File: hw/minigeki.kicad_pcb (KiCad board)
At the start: 2 copper layers, 52 x 56.1 mm, 29 parts, among them J1 USB_C_Receptacle_USB2.0, J2 Conn_01x02, U1 NCP1117-3.3_SOT223, U2 W25Q128JVS, U3 RP2040, Y1 ABLS-12.000MHZ-B4-T

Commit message: hw: finish main routing
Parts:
- added C17: 100n, Capacitor_SMD:C_0402_1005Metric, F.Cu at (52.7, 87.0)
- added C18: 100n, Capacitor_SMD:C_0402_1005Metric, B.Cu at (37.5, 106.0)
- added C19: 100n, Capacitor_SMD:C_0402_1005Metric, F.Cu at (43.8, 137.8)
- added C20: 100n, Capacitor_SMD:C_0402_1005Metric, F.Cu at (62.9, 137.8)
- added C21: 100n, Capacitor_SMD:C_0402_1005Metric, F.Cu at (81.9, 137.8)
- added C22: 100n, Capacitor_SMD:C_0402_1005Metric, F.Cu at (120.0, 137.8)
- added C23: 100n, Capacitor_SMD:C_0402_1005Metric, F.Cu at (139.1, 137.8)
- added C24: 100n, Capacitor_SMD:C_0402_1005Metric, F.Cu at (158.1, 137.8)
- added C25: 100n, Capacitor_SMD:C_0402_1005Metric, B.Cu at (165.7, 107.3)
- added C26: 100n, Capacitor_SMD:C_0402_1005Metric, F.Cu at (156.8, 87.0)
- added D1: SK6812MINI, LED_SMD:LED_SK6812MINI_PLCC4_3.5x3.5mm_P1.75mm, F.Cu at (49.5, 90.2)
- added D10: SK6812MINI, LED_SMD:LED_SK6812MINI_PLCC4_3.5x3.5mm_P1.75mm, F.Cu at (153.7, 90.2)
- added D2: SK6812MINI, LED_SMD:LED_SK6812MINI_PLCC4_3.5x3.5mm_P1.75mm, B.Cu at (34.3, 106.7)
- added D3: SK6812MINI, LED_SMD:LED_SK6812MINI_PLCC4_3.5x3.5mm_P1.75mm, F.Cu at (44.5, 134.6)
- added D4: SK6812MINI, LED_SMD:LED_SK6812MINI_PLCC4_3.5x3.5mm_P1.75mm, F.Cu at (63.5, 134.6)
- added D5: SK6812MINI, LED_SMD:LED_SK6812MINI_PLCC4_3.5x3.5mm_P1.75mm, F.Cu at (82.5, 134.6)
- added D6: SK6812MINI, LED_SMD:LED_SK6812MINI_PLCC4_3.5x3.5mm_P1.75mm, F.Cu at (120.7, 134.6)
- added D7: SK6812MINI, LED_SMD:LED_SK6812MINI_PLCC4_3.5x3.5mm_P1.75mm, F.Cu at (139.7, 134.6)
- added D8: SK6812MINI, LED_SMD:LED_SK6812MINI_PLCC4_3.5x3.5mm_P1.75mm, F.Cu at (158.8, 134.7)
- added D9: SK6812MINI, LED_SMD:LED_SK6812MINI_PLCC4_3.5x3.5mm_P1.75mm, B.Cu at (168.9, 106.7)
- added RV1: PTA4543-2015DPB103, PTAXX33:PTAXX43, F.Cu at (101.6, 101.6)
- added STAB1: Stabilizer_Cherry_MX_2.00u, Mounting_Keyboard_Stabilizer:Stabilizer_Cherry_MX_2.00u, F.Cu at (49.5, 84.5)
- added STAB2: Stabilizer_Cherry_MX_2.00u, Mounting_Keyboard_Stabilizer:Stabilizer_Cherry_MX_2.00u, F.Cu at (153.7, 84.5)
- added SW1: LEFT_R, Switch_Keyboard_Hotswap_Kailh:SW_Hotswap_Kailh_MX_1.00u, F.Cu at (44.5, 129.5)
- added SW10: RIGHT_WALL, Switch_Keyboard_Hotswap_Kailh:SW_Hotswap_Kailh_MX_2.00u, F.Cu at (153.7, 85.1)
- added SW11: MACRO_1, Button_Switch_SMD:SW_SPST_PTS810, F.Cu at (49.5, 106.7)
- added SW12: MACRO_2, Button_Switch_SMD:SW_SPST_PTS810, F.Cu at (153.7, 106.7)
- added SW2: LEFT_G, Switch_Keyboard_Hotswap_Kailh:SW_Hotswap_Kailh_MX_1.00u, F.Cu at (63.5, 129.5)
- added SW3: LEFT_B, Switch_Keyboard_Hotswap_Kailh:SW_Hotswap_Kailh_MX_1.00u, F.Cu at (82.5, 129.5)
- added SW4: LEFT_START, Switch_Keyboard_Hotswap_Kailh:SW_Hotswap_Kailh_MX_1.00u, F.Cu at (81.3, 76.2)
- added SW5: LEFT_WALL, Switch_Keyboard_Hotswap_Kailh:SW_Hotswap_Kailh_MX_2.00u, F.Cu at (49.5, 85.1)
- added SW6: RIGHT_R, Switch_Keyboard_Hotswap_Kailh:SW_Hotswap_Kailh_MX_1.00u, F.Cu at (120.7, 129.5)
- added SW7: RIGHT_G, Switch_Keyboard_Hotswap_Kailh:SW_Hotswap_Kailh_MX_1.00u, F.Cu at (139.7, 129.5)
- added SW8: RIGHT_B, Switch_Keyboard_Hotswap_Kailh:SW_Hotswap_Kailh_MX_1.00u, F.Cu at (158.8, 129.5)
- added SW9: RIGHT_START, Switch_Keyboard_Hotswap_Kailh:SW_Hotswap_Kailh_MX_1.00u, F.Cu at (121.9, 76.2)
- C1, C10, C11, C12, C13, C14, C15, C16, C2, C3, C4, C5, C6, C7, C8, C9, J1, J2, R1, R2, R3, R4, R5, R6, R7, U1, U2, U3, Y1: moved to B.Cu
- moved R2 21.0 mm to (110.5, 82.3)
- moved C4 18.1 mm to (91.0, 89.0), turned to 180 degrees
- moved R1 18.0 mm to (109.0, 82.3)
- moved U1 16.0 mm to (92.0, 82.8)
- moved C1 15.9 mm to (92.1, 76.5), turned to 180 degrees
- moved J2 15.5 mm to (106.6, 77.3), turned to 90 degrees
- moved U2 13.9 mm to (107.0, 87.3), turned to 180 degrees
- moved R6 13.8 mm to (93.1, 70.3)
- moved C11 13.0 mm to (106.5, 97.0), turned to 0 degrees
- moved C12 13.0 mm to (93.5, 101.2), turned to 180 degrees
- moved C13 13.0 mm to (106.5, 101.2), turned to 0 degrees
- moved C15 13.0 mm to (93.5, 96.0), turned to 180 degrees
- moved C16 13.0 mm to (93.5, 94.6), turned to 180 degrees
- moved R7 11.1 mm to (105.6, 70.3)
- moved C10 8.00 mm to (96.0, 93.5)
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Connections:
- U3 pad 11: /GPIO8 -> unconnected-(U3-Pad11)
- U3 pad 12: /GPIO9 -> unconnected-(U3-Pad12)
- U3 pad 13: /GPIO10 -> unconnected-(U3-Pad13)
- U3 pad 14: /GPIO11 -> unconnected-(U3-Pad14)
- U3 pad 15: /GPIO12 -> /RIGHT_B
- U3 pad 16: /GPIO13 -> /RIGHT_G
- U3 pad 17: /GPIO14 -> /RIGHT_R
- U3 pad 18: /GPIO15 -> unconnected-(U3-Pad18)
- U3 pad 2: /GPIO0 -> unconnected-(U3-Pad2)
- U3 pad 27: /GPIO16 -> unconnected-(U3-Pad27)
- U3 pad 28: /GPIO17 -> unconnected-(U3-Pad28)
- U3 pad 29: /GPIO18 -> /LEFT_B
- U3 pad 3: /GPIO1 -> unconnected-(U3-Pad3)
- U3 pad 30: /GPIO19 -> /LEFT_G
- U3 pad 31: /GPIO20 -> /LEFT_R
- U3 pad 32: /GPIO21 -> unconnected-(U3-Pad32)
- U3 pad 34: /GPIO22 -> unconnected-(U3-Pad34)
- U3 pad 35: /GPIO23 -> unconnected-(U3-Pad35)
- U3 pad 36: /GPIO24 -> /LED_DIN
- U3 pad 37: /GPIO25 -> unconnected-(U3-Pad37)
- U3 pad 39: /GPIO27_ADC1 -> /MACRO_1
- U3 pad 4: /GPIO2 -> unconnected-(U3-Pad4)
- U3 pad 40: /GPIO28_ADC2 -> /LEFT_WALL
- U3 pad 41: /GPIO29_ADC3 -> /LEFT_START
- U3 pad 5: /GPIO3 -> unconnected-(U3-Pad5)
- U3 pad 6: /GPIO4 -> /RIGHT_START
- U3 pad 7: /GPIO5 -> /RIGHT_WALL
- U3 pad 8: /GPIO6 -> /MACRO2
- U3 pad 9: /GPIO7 -> unconnected-(U3-Pad9)
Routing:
- net /LEFT_R: track 0.00 -> 74.1 mm
- net /LEFT_WALL: track 0.00 -> 61.9 mm
- net /RIGHT_B: track 0.00 -> 60.0 mm
- net /LEFT_G: track 0.00 -> 51.5 mm
- net /MACRO2: track 0.00 -> 50.4 mm, vias 0 -> 1
- net /RIGHT_WALL: track 0.00 -> 50.3 mm
- net /LED_DIN: track 0.00 -> 49.6 mm, vias 0 -> 1
- net /MACRO_1: track 0.00 -> 47.9 mm, vias 0 -> 1
- net /RIGHT_G: track 0.00 -> 41.0 mm
- net Net-(D5-Pad1): track 0.00 -> 35.3 mm
- net /LEFT_START: track 0.00 -> 35.2 mm
- net /LEFT_B: track 0.00 -> 33.4 mm
- net Net-(D8-Pad1): track 0.00 -> 33.4 mm, vias 0 -> 1
- net /RIGHT_START: track 0.00 -> 32.6 mm
- net Net-(D2-Pad1): track 0.00 -> 30.8 mm, vias 0 -> 1
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- added copper zone on B.Cu, net +1V1
- added copper zone on B.Cu, net +3V3
- added copper zone on B.Cu, net VBUS
- removed copper zone on F.Cu, net +1V1
- removed copper zone on F.Cu, net +3V3
- removed copper zone on F.Cu, net VBUS
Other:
- board size 52 x 56.1 mm -> 146.7 x 78.2 mm

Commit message: hw: final routing pass
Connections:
- SW5 pad 2: unconnected-(SW5-Pad2) -> GND
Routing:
- net GND: track 52.1 -> 115.6 mm, vias 30 -> 60
- net +3V3: track 48.1 -> 64.1 mm, vias 0 -> 2
- net /MACRO2: track 50.4 -> 54.5 mm
- net /MACRO_1: track 47.9 -> 52.0 mm

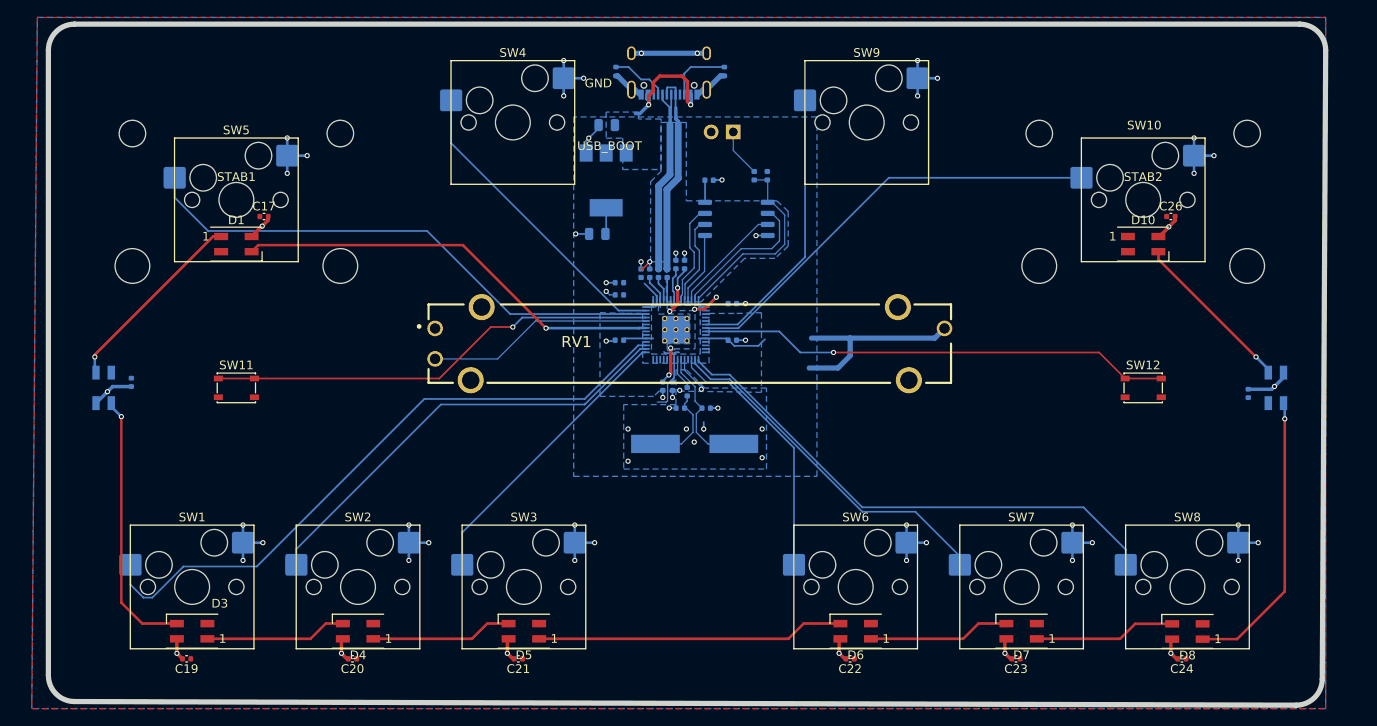
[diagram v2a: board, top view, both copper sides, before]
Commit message: hw: add mounting holes
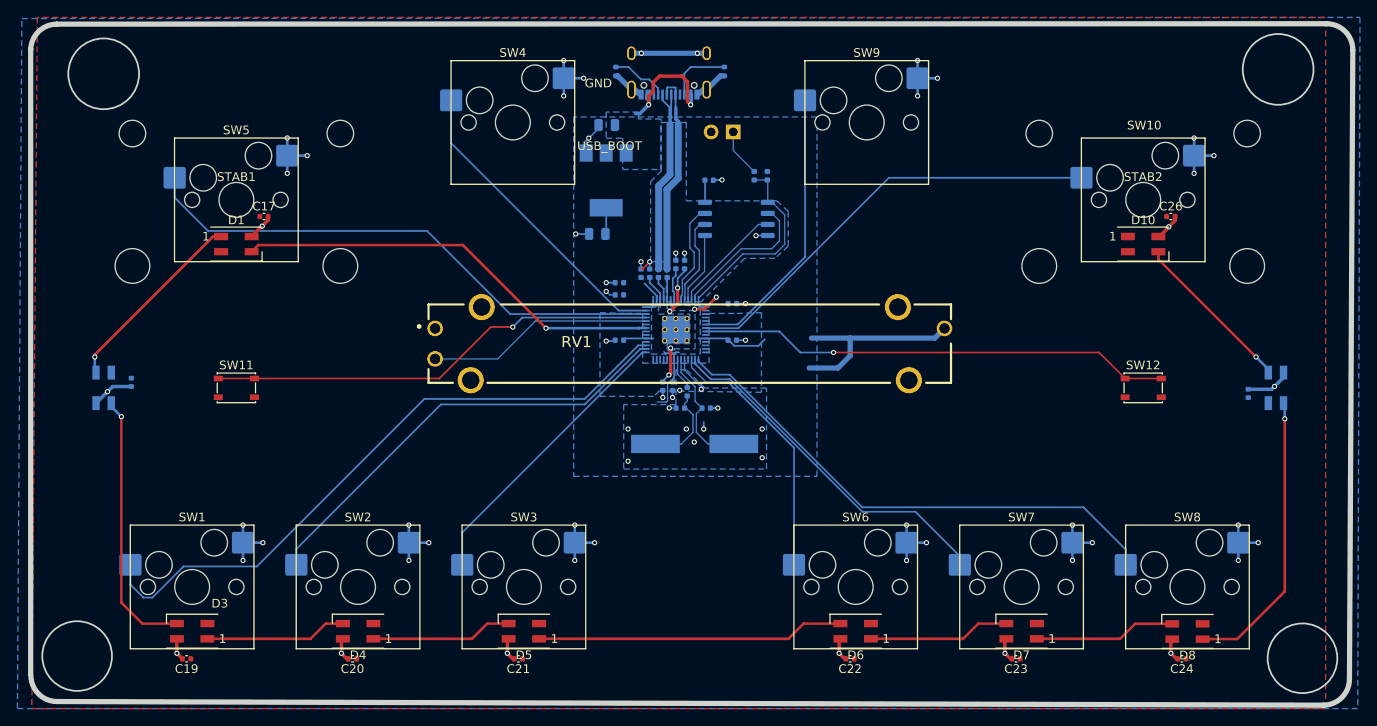
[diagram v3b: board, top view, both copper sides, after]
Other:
- board size 146.7 x 78.2 mm -> 151.8 x 78.3 mm
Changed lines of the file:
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@@
     (fp_line (start -2 0) (end 2 0) (layer "Dwgs.User") (width 0.1))
     (fp_line (start 0 2) (end 0 -2) (layer "Dwgs.User") (width 0.1))
+    (fp_line (start 15.313 -5.53) (end 8.563 -5.53) (layer "Eco1.User") (width 0.1))
     (fp_line (start 15.313 6.77) (end 15.313 -5.53) (layer "Eco1.User") (width 0.1))
+    (fp_line (start -15.313 -5.53) (end -15.313 6.77) (layer "Eco1.User") (width 0.1))
+    (fp_line (start -15.313 6.77) (end -8.563 6.77) (layer "Eco1.User") (width 0.1))
+    (fp_line (start -8.563 6.77) (end -8.563 -5.53) (layer "Eco1.User") (width 0.1))
     (fp_line (start -8.563 -5.53) (end -15.313 -5.53) (layer "Eco1.User") (width 0.1))
     (fp_line (start 8.563 -5.53) (end 8.563 6.77) (layer "Eco1.User") (width 0.1))
-    (fp_line (start -8.563 6.77) (end -8.563 -5.53) (layer "Eco1.User") (width 0.1))
     (fp_line (start 8.563 6.77) (end 15.313 6.77) (layer "Eco1.User") (width 0.1))
-    (fp_line (start -15.313 -5.53) (end -15.313 6.77) (layer "Eco1.User") (width 0.1))
-    (fp_line (start 15.313 -5.53) (end 8.563 -5.53) (layer "Eco1.User") (width 0.1))
-    (fp_line (start -15.313 6.77) (end -8.563 6.77) (layer "Eco1.User") (width 0.1))
     (pad "" np_thru_hole circle locked (at 11.938 -6.985) (size 3.048 3.048) (drill 3.048) (layers *.Cu *.Mask))
+    (pad "" np_thru_hole circle locked (at -11.938 -6.985) (size 3.048 3.048) (drill 3.048) (layers *.Cu *.Mask))
     (pad "" np_thru_hole circle locked (at -11.938 8.225) (size 3.9878 3.9878) (drill 3.9878) (layers *.Cu *.Mask))
     (pad "" np_thru_hole circle locked (at 11.938 8.225) (size 3.9878 3.9878) (drill 3.9878) (layers *.Cu *.Mask))
-    (pad "" np_thru_hole circle locked (at -11.938 -6.985) (size 3.048 3.048) (drill 3.048) (layers *.Cu *.Mask))
     (model "${KICAD6_3RD_PARTY}/3dmodels/com_github_perigoso_keyswitch-kicad-library/3d-library.3dshapes/Stabilizer_Cherry_MX_2.00u.wrl"
       (offset (xyz 0 0 0))
@@
     )
   )
-  (gr_line (start 171.23368 143.11868) (end 30.94 142.7) (layer "Edge.Cuts") (width 0.6))
-  (gr_line (start 174.625 67.90732) (end 174.23368 140.11868) (layer "Edge.Cuts") (width 0.6))
-  (gr_line (start 30.94 64.90732) (end 171.625 64.90732) (layer "Edge.Cuts") (width 0.6))
-  (gr_line (start 27.94 139.7) (end 27.94 67.90732) (layer "Edge.Cuts") (width 0.6))
-  (gr_arc (start 30.94 142.7) (mid 28.81868 141.82132) (end 27.94 139.7) (layer "Edge.Cuts") (width 0.6))
-  (gr_arc (start 174.23368 140.11868) (mid 173.355 142.24) (end 171.23368 143.11868) (layer "Edge.Cuts") (width 0.6))
-  (gr_arc (start 171.625 64.90732) (mid 173.746313 65.786001) (end 174.625 67.90732) (layer "Edge.Cuts") (width 0.6))
-  (gr_arc (start 27.94 67.90732) (mid 28.818673 65.785987) (end 30.94 64.90732) (layer "Edge.Cuts") (width 0.6))
+  (gr_line (start 174.354828 143.11868) (end 28.931328 142.7) (layer "Edge.Cuts") (width 0.6))
+  (gr_line (start 177.74166 67.90732) (end 177.354828 140.11868) (layer "Edge.Cuts") (width 0.6))
+  (gr_line (start 28.908 64.90732) (end 174.740168 64.86006) (layer "Edge.Cuts") (width 0.6))
+  (gr_line (start 25.908 139.52834) (end 25.908 67.73566) (layer "Edge.Cuts") (width 0.6))
+  (gr_arc (start 28.931328 142.7) (mid 26.810008 141.82132) (end 25.931328 139.7) (layer "Edge.Cuts") (width 0.6))
+  (gr_arc (start 177.354828 140.11868) (mid 176.476154 142.240006) (end 174.354828 143.11868) (layer "Edge.Cuts") (width 0.6))
+  (gr_circle (center 169.164 70.104) (end 173.228 70.104) (layer "Edge.Cuts") (width 0.2) (fill none))
+  (gr_circle (center 171.958 137.732) (end 175.958 137.732) (layer "Edge.Cuts") (width 0.2) (fill none))
+  (gr_circle (center 31.242 137.478) (end 35.242 137.478) (layer "Edge.Cuts") (width 0.2) (fill none))
+  (gr_arc (start 174.740168 64.86006) (mid 176.861481 65.738741) (end 177.740168 67.86006) (layer "Edge.Cuts") (width 0.6))
+  (gr_circle (center 34.29 70.612) (end 38.354 70.612) (layer "Edge.Cuts") (width 0.2) (fill none))
+  (gr_arc (start 25.908 67.90732) (mid 26.786671 65.785991) (end 28.908 64.90732) (layer "Edge.Cuts") (width 0.6))
   (gr_text "\nUSB_BOOT" (at 92.38 78.1) (layer "F.SilkS")
     (effects (font (size 1 1) (thickness 0.15)))
@@
   (gr_text "GND" (at 91.1 71.7) (layer "F.SilkS")
     (effects (font (size 1 1) (thickness 0.15)))
+  )
+  (dimension (type aligned) (layer "Dwgs.User")
+    (pts (xy 25.931328 139.7) (xy 177.354828 140.11868))
+    (height 10.246645)
+    (gr_text "151,4241 mm" (at 101.619724 148.355953 359.8415798) (layer "Dwgs.User")
+      (effects (font (size 1.5 1.5) (thickness 0.3)))
+    )
+    (format (units 3) (units_format 1) (precision 4))
+    (style (thickness 0.2) (arrow_length 1.27) (text_position_mode 0) (extension_height 0.58642) (extension_offset 0.5) keep_text_aligned)
+  )
+  (dimension (type aligned) (layer "Dwgs.User")
+    (pts (xy 174.354828 143.11868) (xy 174.740168 64.86006))
+    (height 10.437768)
+    (gr_text "78,2596 mm" (at 183.185161 104.031901 89.71788185) (layer "Dwgs.User")
+      (effects (font (size 1.5 1.5) (thickness 0.3)))
+    )
+    (format (units 3) (units_format 1) (precision 4))
+    (style (thickness 0.2) (arrow_length 1.27) (text_position_mode 0) (extension_height 0.58642) (extension_offset 0.5) keep_text_aligned)
   )
   (segment (start 96.700001 92.499999) (end 97 92.2) (width 0.2) (layer "F.Cu") (net 1))
@@
     (polygon
       (pts
-        (xy 174.625 143.51)
-        (xy 26.035 143.51)
-        (xy 26.67 64.135)
-        (xy 174.625 64.135)
+        (xy 178.308 143.51)
+        (xy 24.384 143.51)
+        (xy 24.892 64.262)
+        (xy 178.562 64.135)
       )
     )
